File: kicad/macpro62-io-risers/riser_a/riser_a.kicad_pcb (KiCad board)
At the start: 4 copper layers, 21.4 x 21.7 mm, 5 parts, among them J1 A1 kinghelm KH-3.0AF180ZJ-11.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, J10 DF40C-50DS-0.4V(51) TBC riser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, J2 A2 kinghelm KH-3.0AF180ZJ-11.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

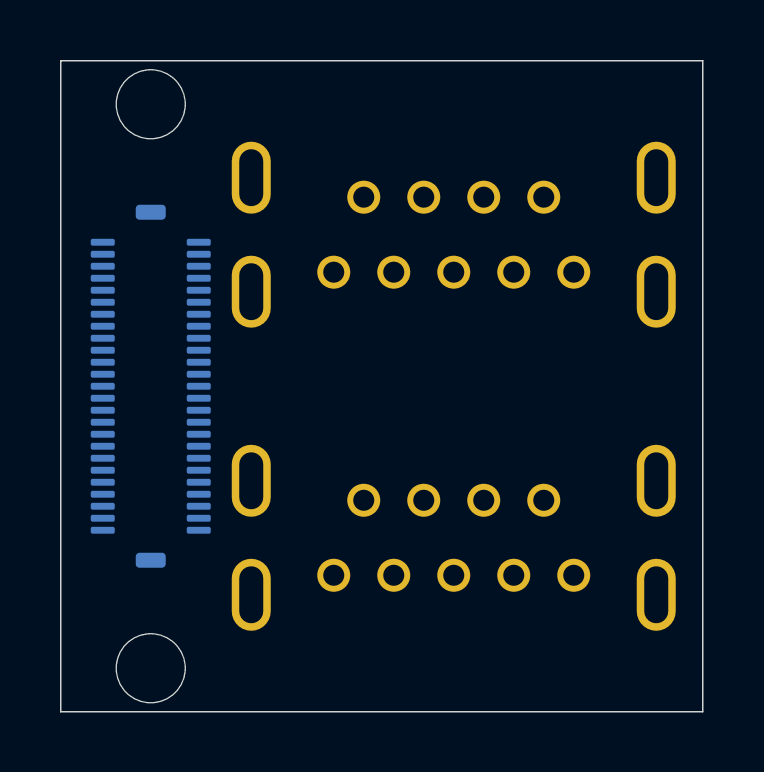
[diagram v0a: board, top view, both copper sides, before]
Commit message: I/O: ports tilted 12.5 deg per stock, riser edge trims, USB-A B2B moved on top, outer-face plug seats, D21-D26 removed
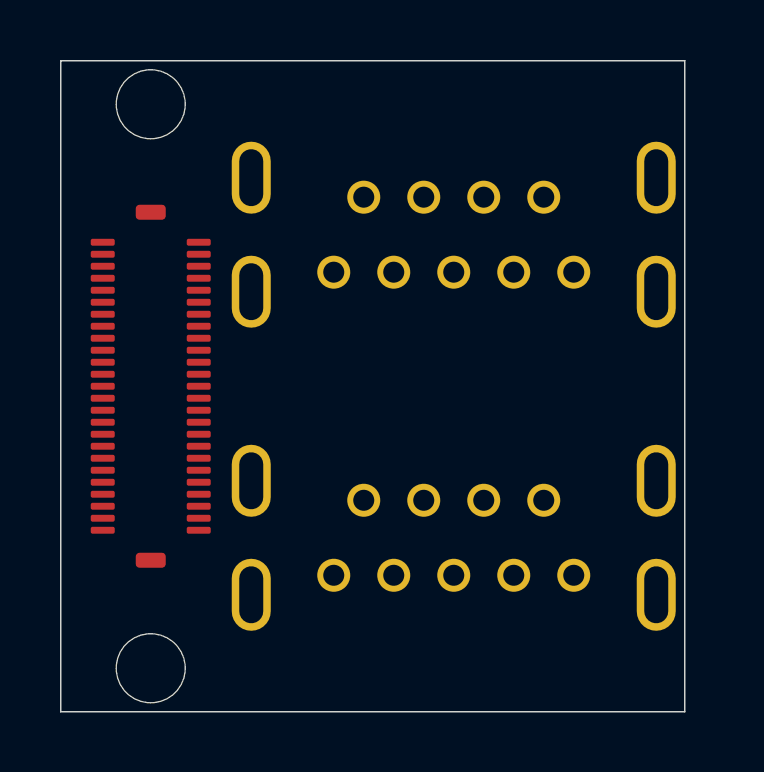
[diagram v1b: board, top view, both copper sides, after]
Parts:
- J1: value A1 kinghelm KH-3.0AF180ZJ-11.5JB (C2979037) (mouth 18.49 above main board top) -> A1 kinghelm KH-3.0AF180ZJ-11.5JB (C2979037) (mouth 17.65 above main board top)
- J10: value DF40C-50DS-0.4V(51) TBC riser side (flex jumper to main JR) -> DF40C-50DS-0.4V(51) TBC riser side (flex jumper to main JR, on the TOP: U-turn round the outboard edge); moved to F.Cu
- J2: value A2 kinghelm KH-3.0AF180ZJ-11.5JB (C2979037) (mouth 18.49 above main board top) -> A2 kinghelm KH-3.0AF180ZJ-11.5JB (C2979037) (mouth 17.65 above main board top)
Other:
- board size 21.4 x 21.7 mm -> 20.8 x 21.7 mm
- board text added: "riser_a A0 12.5 deg"
- board text removed: "riser_a A0 5.2 deg"
